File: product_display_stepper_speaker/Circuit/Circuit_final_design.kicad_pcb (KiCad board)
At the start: 2 copper layers, 89.7 x 50.2 mm, 19 parts, among them J1 Barrel_Jack_MountingPin, U1 L7805, U2 LM2931-3.3_TO220, U3 ESP-12E

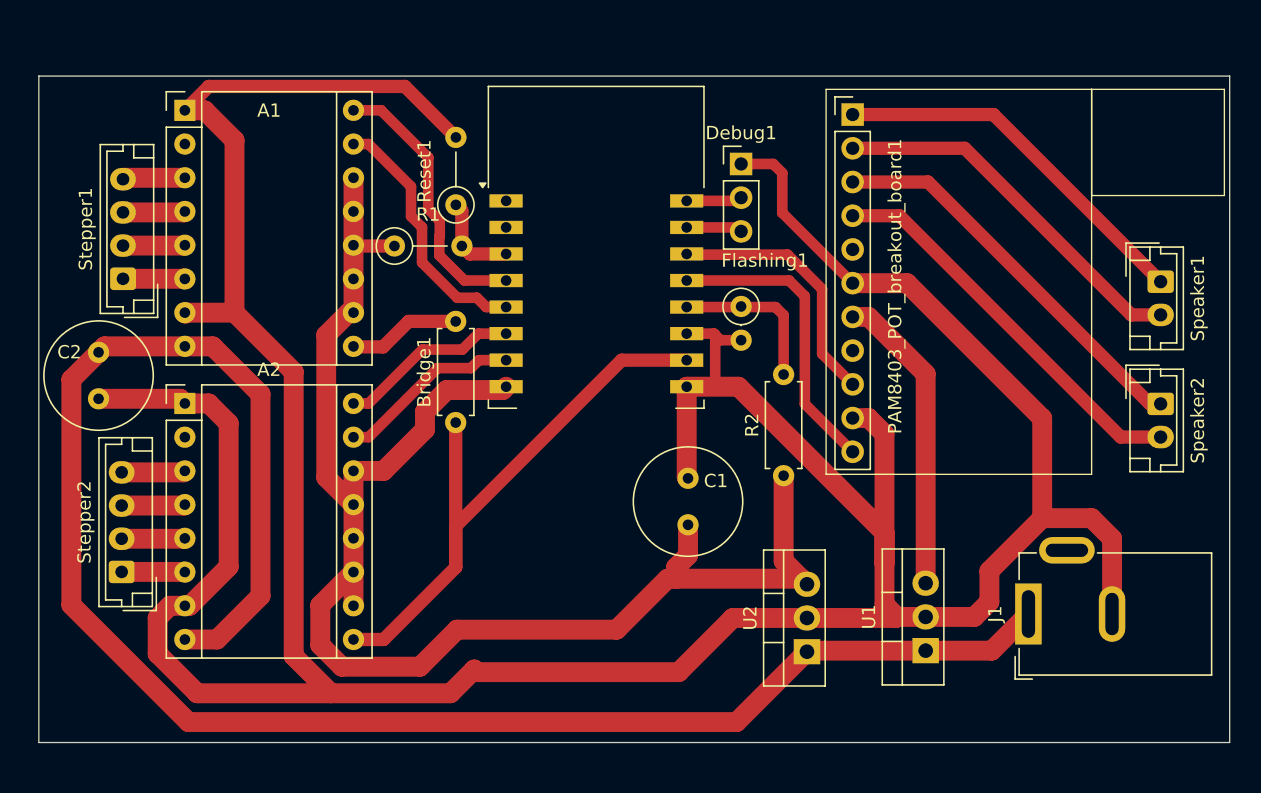
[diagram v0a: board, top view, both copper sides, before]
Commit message: finished circuits of both hospital rover and product display with speakers and steppers projects
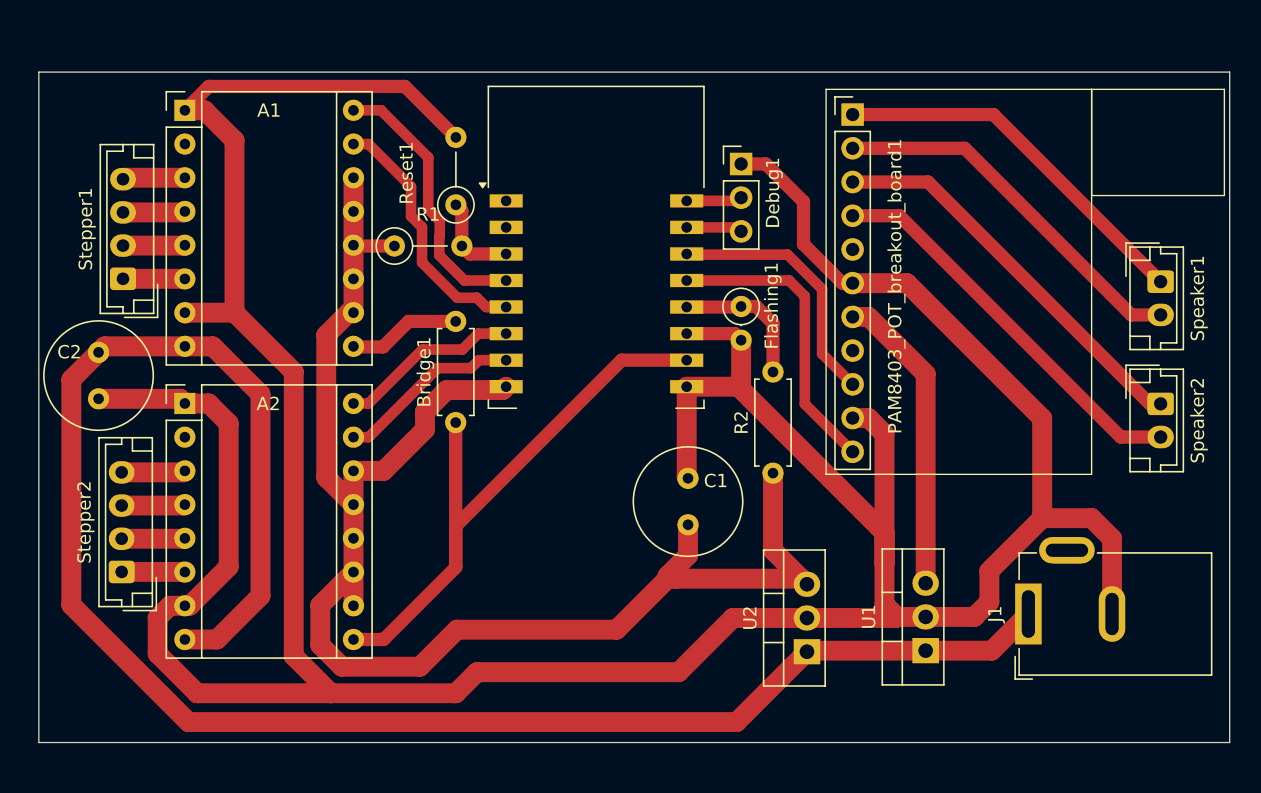
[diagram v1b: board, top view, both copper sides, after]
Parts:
- A1, A2: value Pololu_Breakout_DRV8825 -> DRV8825
- U2: value LM2931-3.3_TO220 -> LD33v
- moved R2 0.82 mm to (145.1, 116.1)
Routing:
- net mode: track 12.0 -> 10.7 mm
- net +3.3V: track 114.8 -> 115.6 mm
- net GND: track 287.4 -> 286.9 mm
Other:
- board size 89.7 x 50.2 mm -> 89.7 x 50.5 mm

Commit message: major circuit fixing for both current projects
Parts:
- added R3: 10k, Resistor_THT:R_Axial_DIN0207_L6.3mm_D2.5mm_P7.62mm_Horizontal, F.Cu at (125.0, 113.9)
- moved Speaker1 10.8 mm to (174.1, 90.9)
- moved Speaker2 10.1 mm to (174.0, 100.8)
- moved U2 4.95 mm to (147.3, 124.6), turned to -90 degrees
- moved Reset1 3.00 mm to (118.8, 94.1)
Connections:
- U2 pad 1: +12V -> GND
- U2 pad 2: GND -> +3.3V
- U2 pad 3: +3.3V -> +12V
- U3 pad 17: GND -> Net-(U3-GPIO2)
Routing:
- net GND: track 286.9 -> 393.1 mm
- net Net-(U3-GPIO2): track 0.00 -> 12.8 mm
- net +3.3V: track 115.6 -> 126.7 mm
- net Net-(PAM8403_POT_breakout_board1-Pin_2): track 28.4 -> 23.7 mm
- net Net-(PAM8403_POT_breakout_board1-Pin_1): track 28.4 -> 23.7 mm
- net Net-(PAM8403_POT_breakout_board1-Pin_4): track 30.1 -> 25.6 mm
- net Net-(PAM8403_POT_breakout_board1-Pin_3): track 30.1 -> 25.6 mm
- net EN: track 46.5 -> 50.0 mm
- net Reset: track 6.87 -> 9.66 mm
- net STEP2: track 19.5 -> 20.0 mm
- net DIR2: track 20.7 -> 21.2 mm
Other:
- board size 89.7 x 50.5 mm -> 90.6 x 52.4 mm

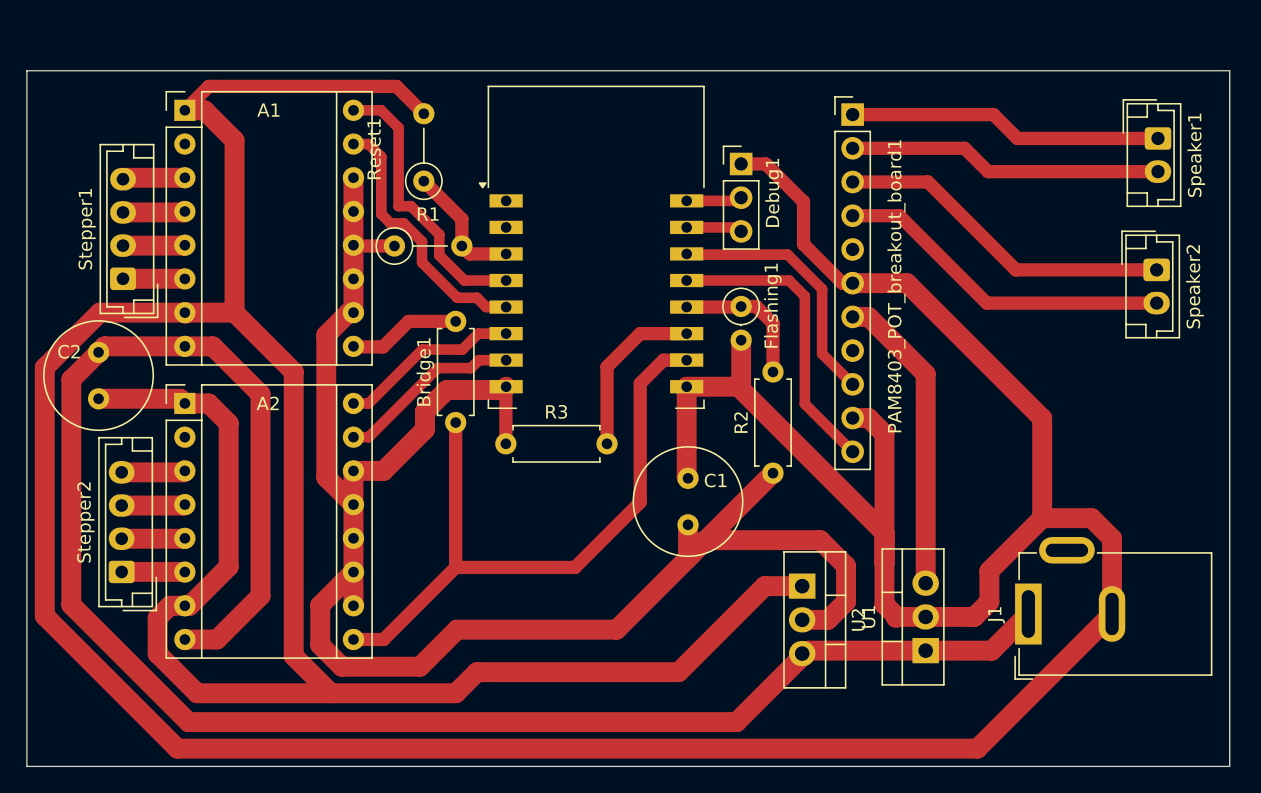
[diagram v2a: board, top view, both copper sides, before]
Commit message: started programming product display stepper speaker project
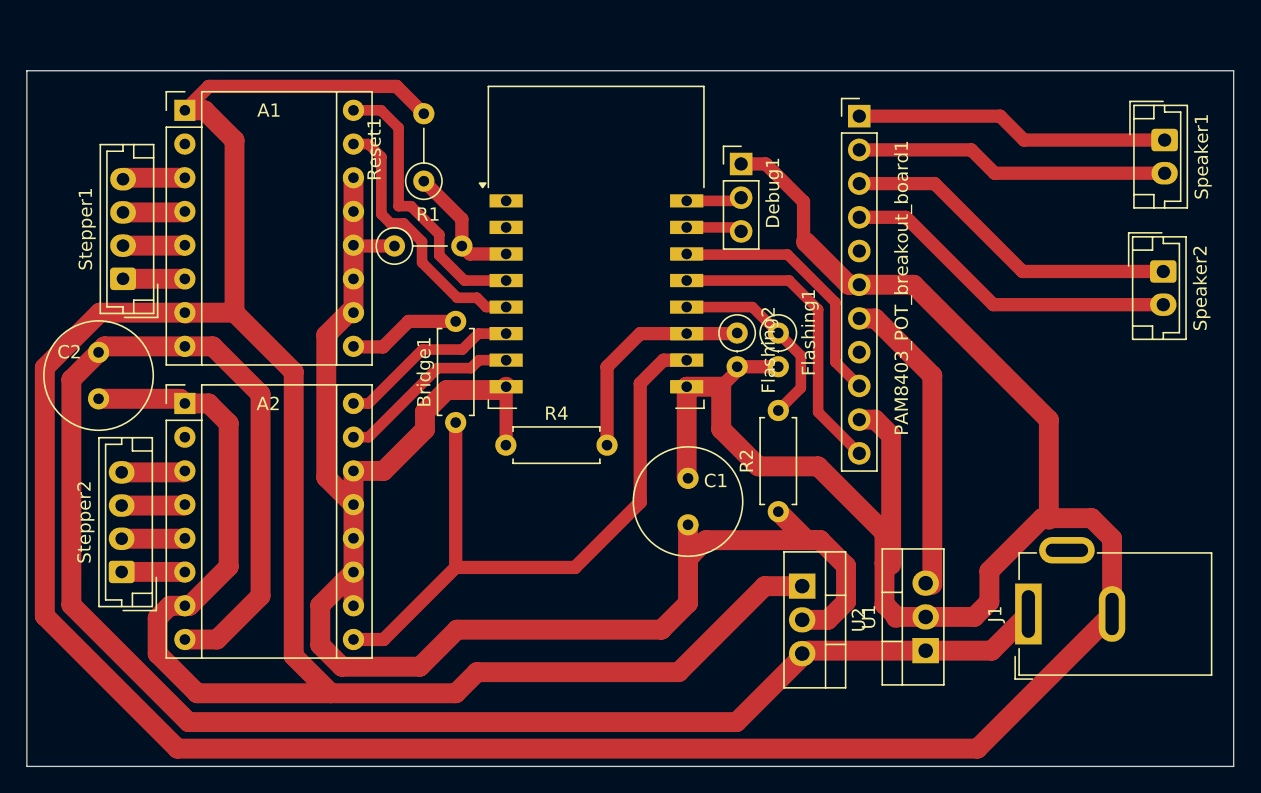
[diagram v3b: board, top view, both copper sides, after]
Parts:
- removed R3: 10k, Resistor_THT:R_Axial_DIN0207_L6.3mm_D2.5mm_P7.62mm_Horizontal
- added Flashing2: Headers, Resistor_THT:R_Axial_DIN0207_L6.3mm_D2.5mm_P2.54mm_Vertical, F.Cu at (142.4, 105.6)
- added R4: 10k, Resistor_THT:R_Axial_DIN0207_L6.3mm_D2.5mm_P7.62mm_Horizontal, F.Cu at (125.0, 114.0)
- moved Flashing1 3.44 mm to (145.5, 105.6)
- moved R2 2.93 mm to (145.5, 119.0)
- moved PAM8403_POT_breakout_board1 0.51 mm to (151.6, 89.2)
- moved Speaker2 0.51 mm to (174.5, 100.9)
- moved Speaker1 0.51 mm to (174.6, 91.0)
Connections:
- net mode renamed mode1
- U3 pad 17: Net-(U3-GPIO2) -> mode2
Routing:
- net mode2: track 0.00 -> 16.8 mm
- net Net-(U3-GPIO2): track 12.8 -> 0.00 mm
- net mode1: track 10.7 -> 15.0 mm
- net GND: track 393.1 -> 396.9 mm
- net +3.3V: track 126.7 -> 125.7 mm
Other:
- board size 90.6 x 52.4 mm -> 90.9 x 52.4 mm

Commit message: added circuit step files for both current projects
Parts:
- A1, A2: footprint Module:Pololu_Breakout-16_15.2x20.3mm -> DRV8825:DRV8825_module
- moved A1 11.0 mm to (107.3, 97.7)
- moved A2 11.0 mm to (107.3, 119.8)
